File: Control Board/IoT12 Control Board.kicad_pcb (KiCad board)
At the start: 2 copper layers, 99.1 x 69.8 mm, 114 parts, among them J10 USB_B_Micro, J11 Conn_ARM_JTAG_SWD_10, J9 Conn_ARM_JTAG_SWD_10, Q1 MMBT2222, Q2 MMBT2222, Q3 AOD403, SW1 Rotary encoder EC11 Plum 15mm, SW2 SW_Push, U1 ATSAMD21G18A-AU, U2 ADS1115IDGS, U3 INA826AID, U4 INA826AID, U5 LM2596S-ADJ, U6 AT24C32, U7 MAX809S, Y1 32768Hz

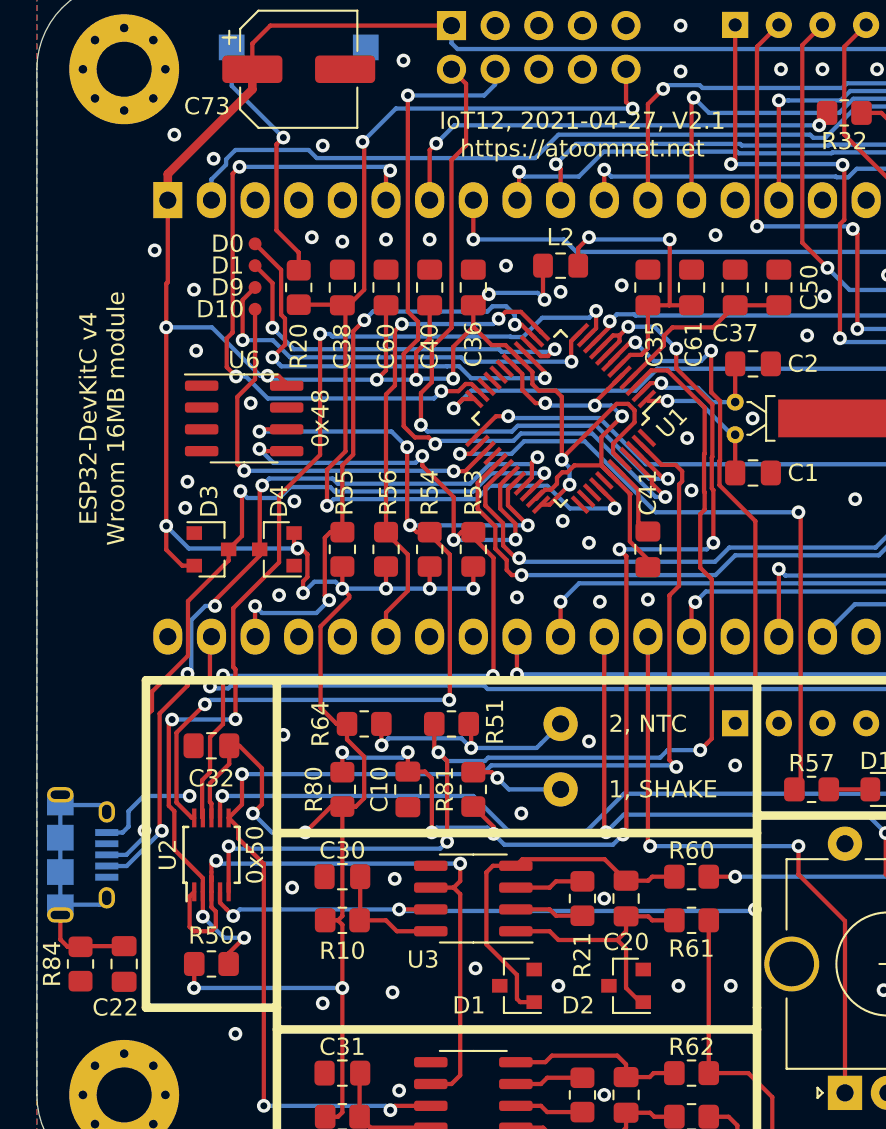
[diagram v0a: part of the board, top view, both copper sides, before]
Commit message: Remove capacitor and resistor from usb shield.
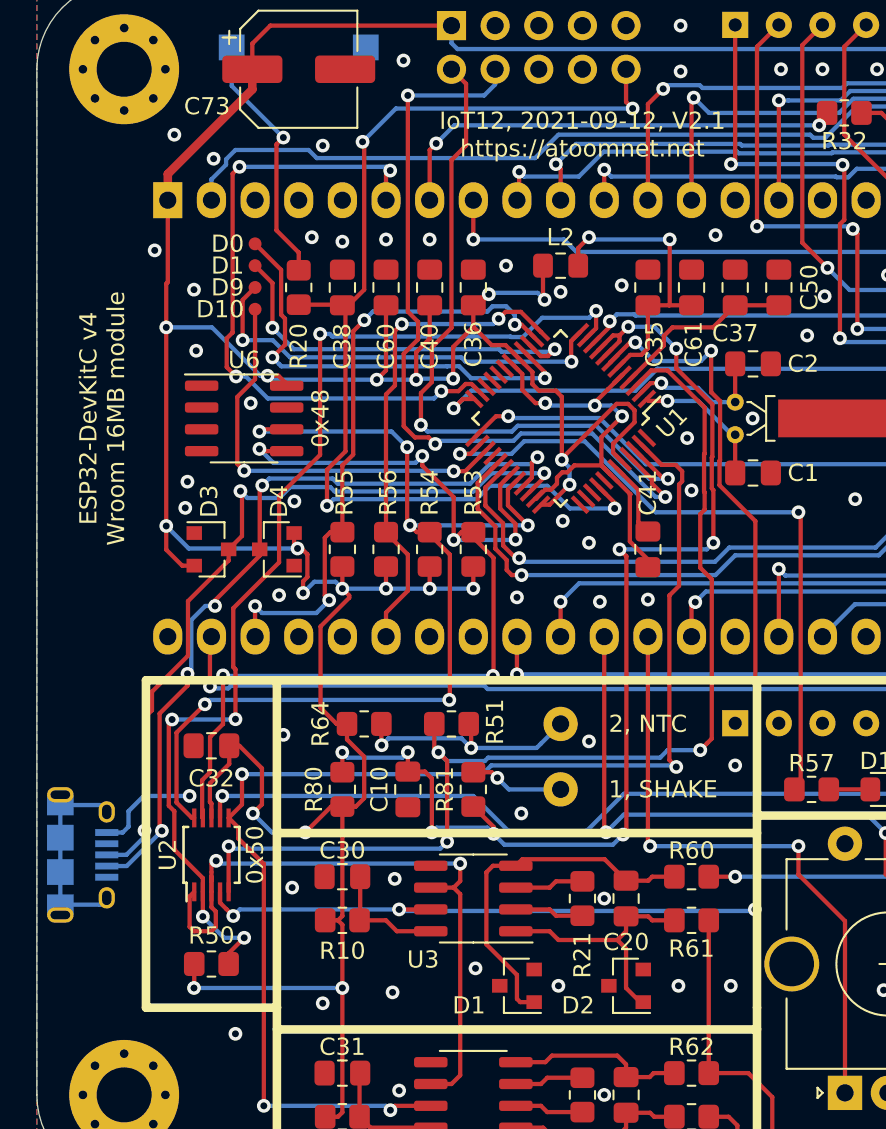
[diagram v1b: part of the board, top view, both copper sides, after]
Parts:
- removed C22: 1nF, Capacitor_SMD:C_0805_2012Metric_Pad1.18x1.45mm_HandSolder
- removed R84: 1M, Resistor_SMD:R_0805_2012Metric_Pad1.20x1.40mm_HandSolder
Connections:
- J10 pad : (no net) -> Net-(J10-Pad6)
- J10 pad 6: Net-(C22-Pad1) -> Net-(J10-Pad6)
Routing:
- net Net-(C22-Pad1): track 18.1 -> 0.00 mm
- net Net-(J10-Pad6): track 0.00 -> 12.7 mm
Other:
- board text added: "IoT12, 2021-09-12, V2.1 https://atoomnet.net"
- board text removed: "IoT12, 2021-04-27, V2.1 https://atoomnet.net"

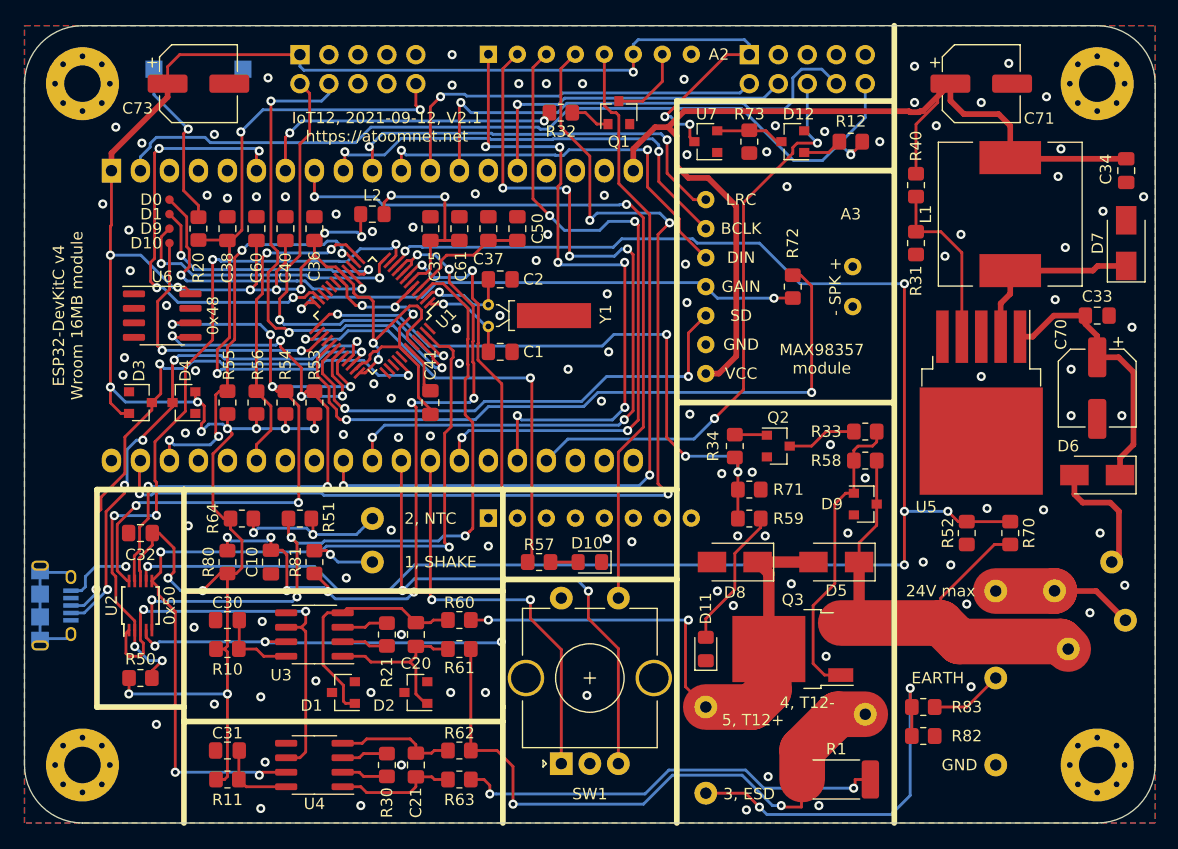
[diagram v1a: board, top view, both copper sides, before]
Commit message: PCB component placement change.
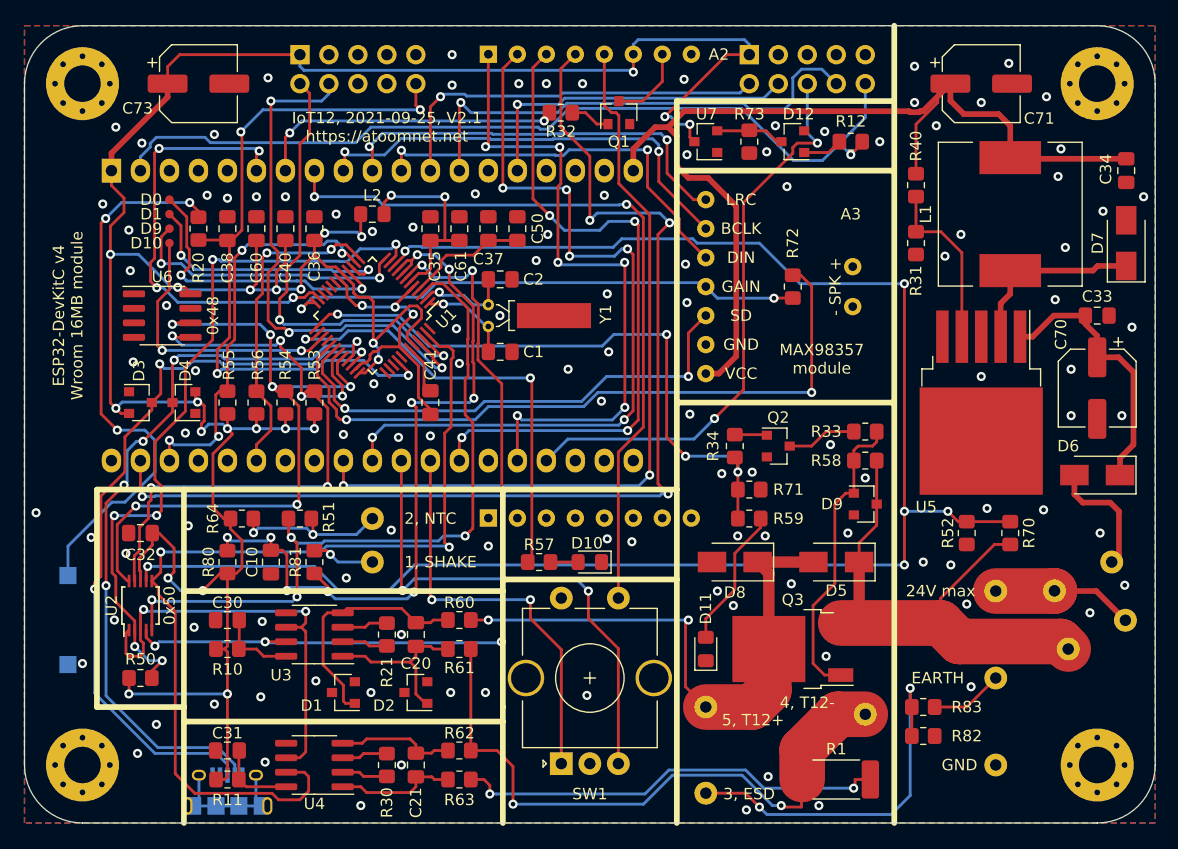
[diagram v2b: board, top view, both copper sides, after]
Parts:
- moved SW2 49.6 mm to (-45.7, 10.2), turned to 90 degrees
- moved J10 22.2 mm to (-31.8, 25.1), turned to 180 degrees
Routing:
- net Net-(R20-Pad1): track 14.9 -> 48.2 mm, vias 1 -> 3
- net /Brain/USB+: track 45.3 -> 66.6 mm
- net /Brain/USB-: track 46.0 -> 65.9 mm
- net IRON_CURRENT: track 76.7 -> 83.2 mm, vias 4 -> 2
- net GND: track 42.0 -> 35.8 mm, vias 117 -> 120
- net Net-(J10-Pad6): track 12.7 -> 11.9 mm
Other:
- board text added: "IoT12, 2021-09-25, V2.1 https://atoomnet.net"
- board text removed: "IoT12, 2021-09-12, V2.1 https://atoomnet.net"
- board text removed: "Q: If the Continuum's told you once, they've told you a thousand times. DON'T - PROVOKE - THE BORG!!"

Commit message: Add LCD pin labels. Add testpoints heat controller.
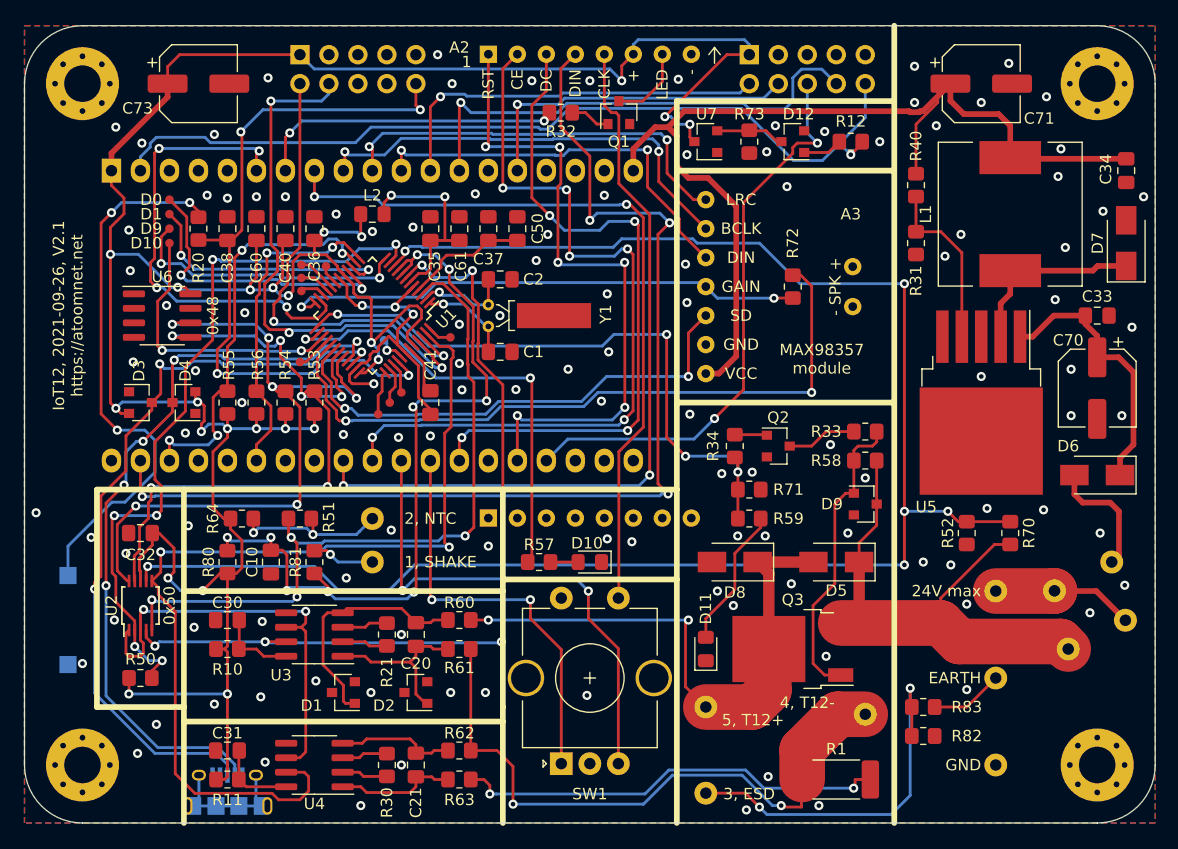
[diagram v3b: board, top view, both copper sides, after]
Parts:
- added TP10: TestPoint, TestPoint-extra:TestPoint_Pad_D0.75mm, F.Cu at (-16.5, -9.78)
- added TP11: TestPoint, TestPoint-extra:TestPoint_Pad_D0.75mm, F.Cu at (-25.3, -18.7)
- added TP12: TestPoint, TestPoint-extra:TestPoint_Pad_D0.75mm, F.Cu at (-18.5, -7.87)
- added TP13: TestPoint, TestPoint-extra:TestPoint_Pad_D0.75mm, F.Cu at (-17.5, -8.89)
- added TP14: TestPoint, TestPoint-extra:TestPoint_Pad_D0.75mm, B.Cu at (-18.0, -14.4)
- added TP5: TestPoint, TestPoint-extra:TestPoint_Pad_D0.75mm, F.Cu at (-25.4, -12.4)
- added TP6: TestPoint, TestPoint-extra:TestPoint_Pad_D0.75mm, F.Cu at (-25.3, -19.8)
- added TP7: TestPoint, TestPoint-extra:TestPoint_Pad_D0.75mm, F.Cu at (-23.1, -20.8)
- added TP8: TestPoint, TestPoint-extra:TestPoint_Pad_D0.75mm, F.Cu at (-25.3, -21.0)
- added TP9: TestPoint, TestPoint-extra:TestPoint_Pad_D0.75mm, F.Cu at (-12.2, -14.6)
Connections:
- J10 pad : Net-(J10-Pad6) -> (no net)
- U1 pad 19: Net-(U1-Pad19) -> /Brain/PB10
- U1 pad 20: Net-(U1-Pad20) -> /Brain/PB11
- U1 pad 21: Net-(U1-Pad21) -> /Brain/PA12
- U1 pad 22: Net-(U1-Pad22) -> /Brain/ATN
- U1 pad 28: Net-(U1-Pad28) -> /Brain/D12
- U1 pad 37: Net-(U1-Pad37) -> /Brain/PB22
- U1 pad 38: Net-(U1-Pad38) -> /Brain/PB23
- U1 pad 39: Net-(U1-Pad39) -> /Brain/PA27
- U1 pad 41: Net-(U1-Pad41) -> /Brain/PA28
- U1 pad 48: Net-(U1-Pad48) -> /Brain/PB03
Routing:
- net /Brain/PB22: track 0.00 -> 3.87 mm
- net GND: track 35.8 -> 39.4 mm, vias 120 -> 121
- net /Brain/PB11: track 0.00 -> 3.40 mm
- net /Brain/PB23: track 0.00 -> 3.37 mm
- net /Brain/D12: track 0.00 -> 3.17 mm
- net /Brain/PA12: track 0.00 -> 2.72 mm
- net /Brain/PA27: track 0.00 -> 2.71 mm
- net /Brain/PA28: track 0.00 -> 2.50 mm, vias 0 -> 1
- net HEAT_INT: track 38.7 -> 41.2 mm
- net /Brain/ATN: track 0.00 -> 2.21 mm
- net /Brain/PB03: track 0.00 -> 2.13 mm
- net HEAT_SCL: track 59.2 -> 61.3 mm
- net /Brain/PB10: track 0.00 -> 1.75 mm
- net AIN_COMP: track 66.9 -> 68.3 mm
- net +3V3: track 258.2 -> 259.0 mm
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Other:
- board text added: "+"
- board text added: "-"
- board text added: "1"
- board text added: "CE"
- board text added: "CLK"
- board text added: "DC"
- board text added: "DIN"
- board text added: "IoT12, 2021-09-26, V2.1 https://atoomnet.net"
- board text added: "LED"
- board text added: "RST"
- board text removed: "IoT12, 2021-09-25, V2.1 https://atoomnet.net"
